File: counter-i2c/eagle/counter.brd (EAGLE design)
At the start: 126.2 x 32 mm, 76 parts, among them IC1 MCP1703DB, IC2 4067D, IC3 74HC154DW, J1 RJ12RIGHTANGLE-I2C, X2 8MHz, X4 MINI-USB

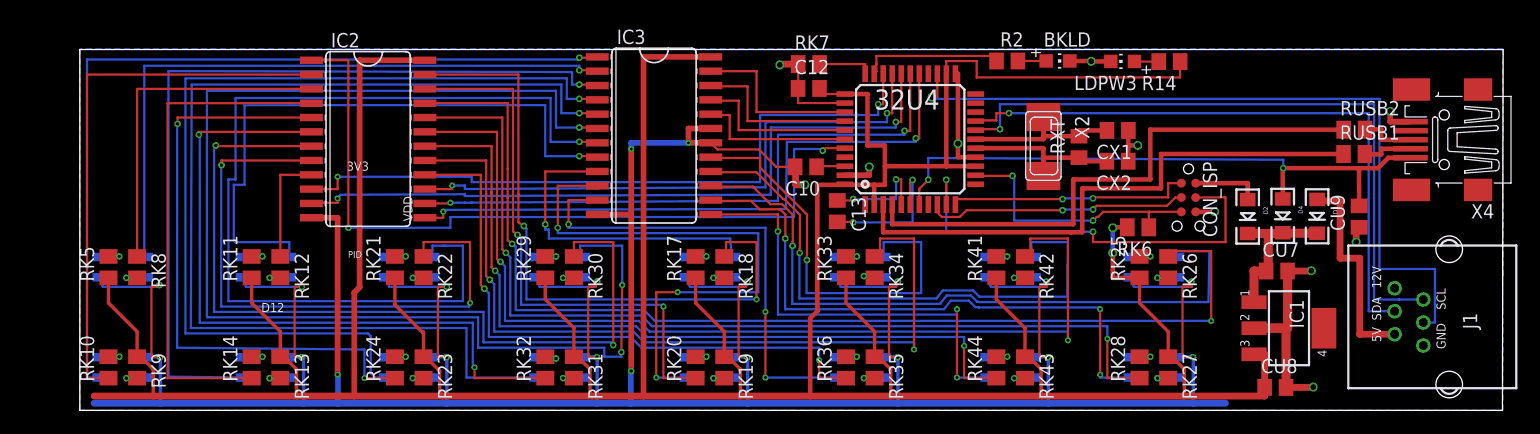
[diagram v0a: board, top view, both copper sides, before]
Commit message: master: fix parameter for logging interval
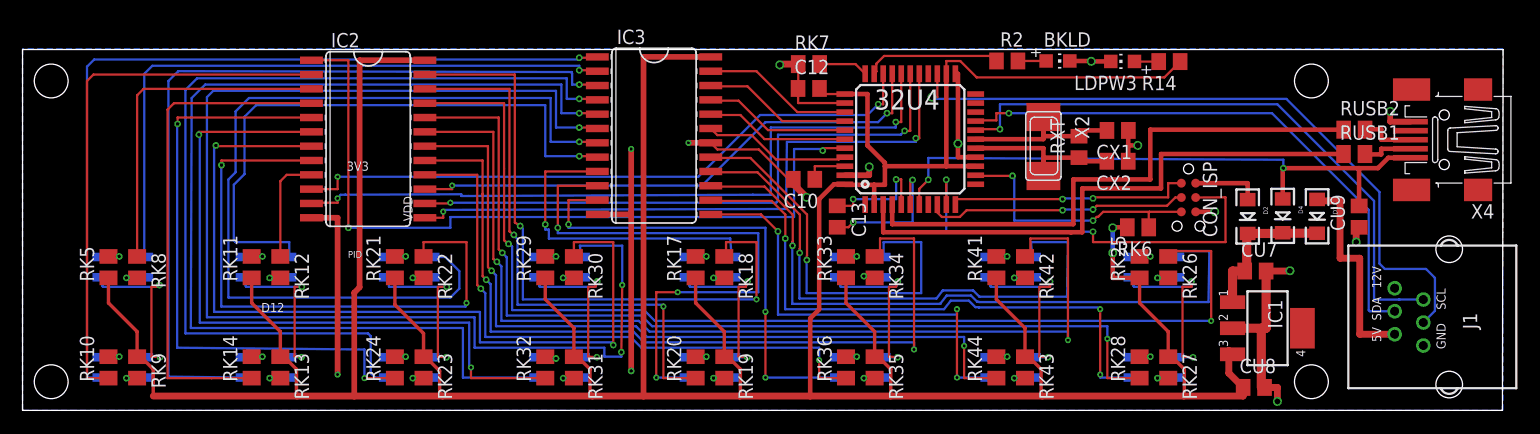
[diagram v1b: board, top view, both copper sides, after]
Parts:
- moved IC1 1.91 mm to (105.3, 7.28)
- moved CU7 1.90 mm to (104.3, 12.4)
- moved CU8 1.90 mm to (104.1, 2.03)
- moved C10 1.12 mm to (64.2, 20.5)
- moved C13 0.48 mm to (67.2, 17.2)
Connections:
- net A5: now also IC3.19
- net GND: no longer IC3.19
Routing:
- net GND: track 399.2 -> 237.1 mm
- net A5: track 0.00 -> 13.1 mm
- net 3.3V: track 369.5 -> 359.0 mm
- net A6: track 68.2 -> 62.0 mm
- net DMUX5: track 84.3 -> 78.7 mm
- net SDA: track 55.5 -> 50.4 mm
- net SCL: track 59.3 -> 54.3 mm
- net D5*: track 61.9 -> 57.2 mm
- net D10*: track 52.2 -> 47.9 mm
- net A0: track 15.5 -> 13.4 mm
- net A1: track 15.0 -> 13.2 mm
- net A2: track 14.6 -> 13.0 mm
- net DMUX3: track 55.5 -> 54.0 mm
- net A3: track 14.1 -> 12.8 mm
- net AREF: track 2.56 -> 3.83 mm
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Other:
- board size 126.2 x 32 mm -> 131.3 x 32 mm

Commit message: close #19
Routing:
- net GND: track 237.1 -> 223.2 mm, vias 33 -> 32
